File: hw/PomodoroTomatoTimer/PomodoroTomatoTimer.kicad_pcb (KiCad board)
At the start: 2 copper layers, 25.4 x 25.4 mm, 19 parts, among them J1 Coin Cell, SW1 SW_DIP_x02, U1 STM32F030F4Px

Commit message: + Placement and routing ok.
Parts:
- added Q1: BSS83P, Package_TO_SOT_SMD:SOT-23, F.Cu at (130.8, 88.6)
- added Q2: 2N7002, Package_TO_SOT_SMD:SOT-23, F.Cu at (129.3, 85.1)
- added Q3: BC807, Package_TO_SOT_SMD:SOT-23, F.Cu at (135.9, 97.8)
- added Q4: BSS83P, Package_TO_SOT_SMD:SOT-23, F.Cu at (139.4, 97.8)
- added Q5: BC807, Package_TO_SOT_SMD:SOT-23, F.Cu at (143.0, 97.8)
- added R10: 47k 0603, Resistor_SMD:R_0603_1608Metric, F.Cu at (133.3, 99.5)
- added R11: 10k 0603, Resistor_SMD:R_0603_1608Metric, F.Cu at (131.7, 85.2)
- added R12: 47k 0603, Resistor_SMD:R_0603_1608Metric, F.Cu at (139.2, 100.3)
- added R8: 10k 0603, Resistor_SMD:R_0603_1608Metric, F.Cu at (128.3, 88.9)
- added R9: 10k 0603, Resistor_SMD:R_0603_1608Metric, F.Cu at (135.9, 100.3)
- SW1: value SW_DIP_x02 -> SW_DPST_x2
- moved C4 23.2 mm to (128.8, 94.1), turned to 45 degrees
- moved C3 18.9 mm to (129.3, 95.6), turned to 45 degrees
- moved R1 18.1 mm to (147.7, 98.7)
- moved R2 17.1 mm to (145.4, 99.2), turned to 90 degrees
- moved D4 15.6 mm to (144.3, 79.2), turned to 270 degrees
- moved D5 15.1 mm to (148.8, 79.2), turned to 270 degrees
- moved R7 14.0 mm to (150.9, 79.2), turned to 270 degrees
- moved C1 12.9 mm to (142.5, 94.5), turned to 270 degrees
- moved U1 12.3 mm to (148.3, 93.8)
- moved C2 11.4 mm to (143.9, 94.5), turned to 270 degrees
- moved SW1 10.5 mm to (136.7, 86.4)
- moved J1 9.20 mm to (130.6, 98.0), turned to 45 degrees
- moved D3 6.03 mm to (139.7, 79.2), turned to 270 degrees
- moved D2 5.98 mm to (135.1, 79.2), turned to 270 degrees
- moved R3 5.70 mm to (132.6, 79.2), turned to 270 degrees
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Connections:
- SW1 pad 1: Net-(SW1-Pad1) -> VDDA
- SW1 pad 2: Net-(SW1-Pad2) -> /BUTTON
- U1 pad 11: Net-(U1-Pad11) -> /LED5
- U1 pad 12: Net-(U1-Pad12) -> /LED4
- U1 pad 13: Net-(U1-Pad13) -> /LED3
- U1 pad 14: Net-(U1-Pad14) -> /LED2
- U1 pad 17: Net-(U1-Pad17) -> /LED1
- U1 pad 20: Net-(U1-Pad20) -> /BUTTON
- U1 pad 6: Net-(U1-Pad6) -> /POW_CTRL
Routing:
- net VDD: track 0.00 -> 40.0 mm, vias 0 -> 2
- net /POW_CTRL: track 0.00 -> 29.3 mm, vias 0 -> 2
- net VDDA: track 0.00 -> 26.6 mm
- net GND: track 0.00 -> 25.3 mm, vias 0 -> 10
- net /BUTTON: track 0.00 -> 21.4 mm
- net /LED1: track 0.00 -> 20.6 mm
- net /LED2: track 0.00 -> 20.4 mm
- net /LED3: track 0.00 -> 16.5 mm
- net /LED4: track 0.00 -> 12.6 mm
- net Net-(Q3-Pad1): track 0.00 -> 11.9 mm, vias 0 -> 2
- net /LED5: track 0.00 -> 11.0 mm
- net Net-(Q4-Pad1): track 0.00 -> 7.94 mm
- net Net-(Q1-Pad1): track 0.00 -> 4.71 mm
- net Net-(D5-Pad2): track 0.00 -> 2.75 mm
- net Net-(D4-Pad2): track 0.00 -> 2.75 mm
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- added copper zone on B.Cu, net GND
- added copper zone on F.Cu, net GND
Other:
- net class Default: clearance 0.2 -> 0.25
- rule trace_clearance: 0.2 -> 0.25

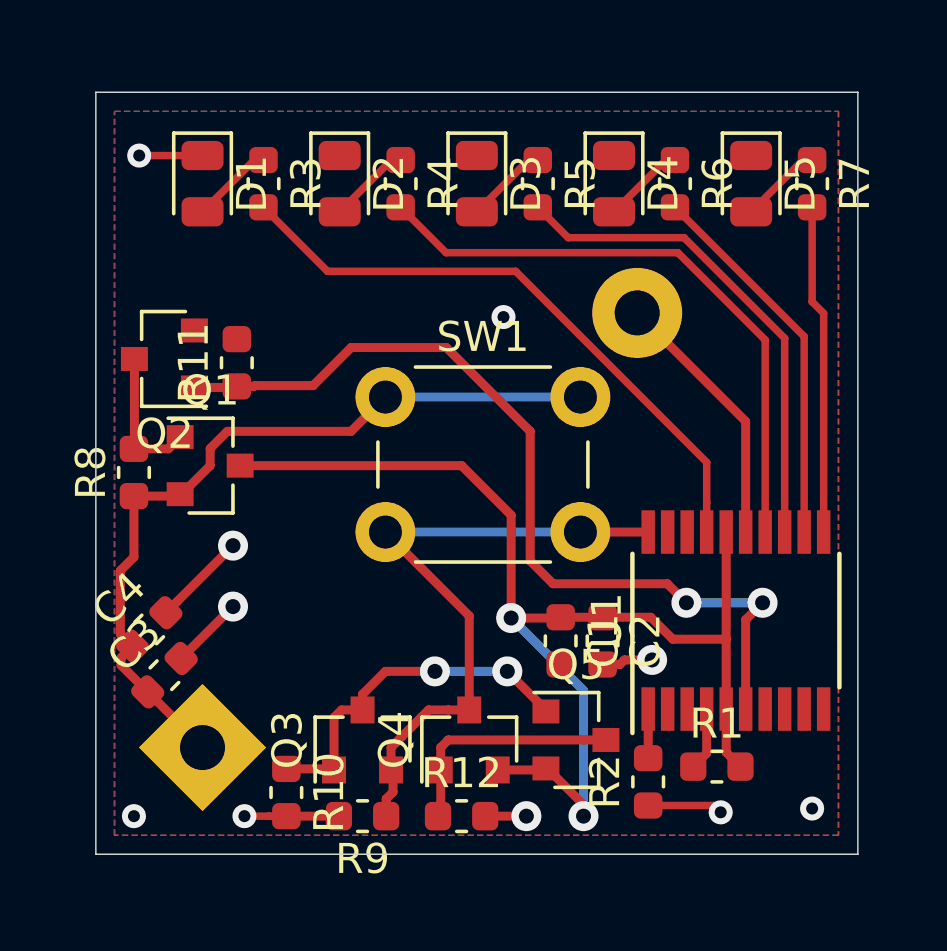
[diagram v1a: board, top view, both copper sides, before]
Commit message: + silk screen updated
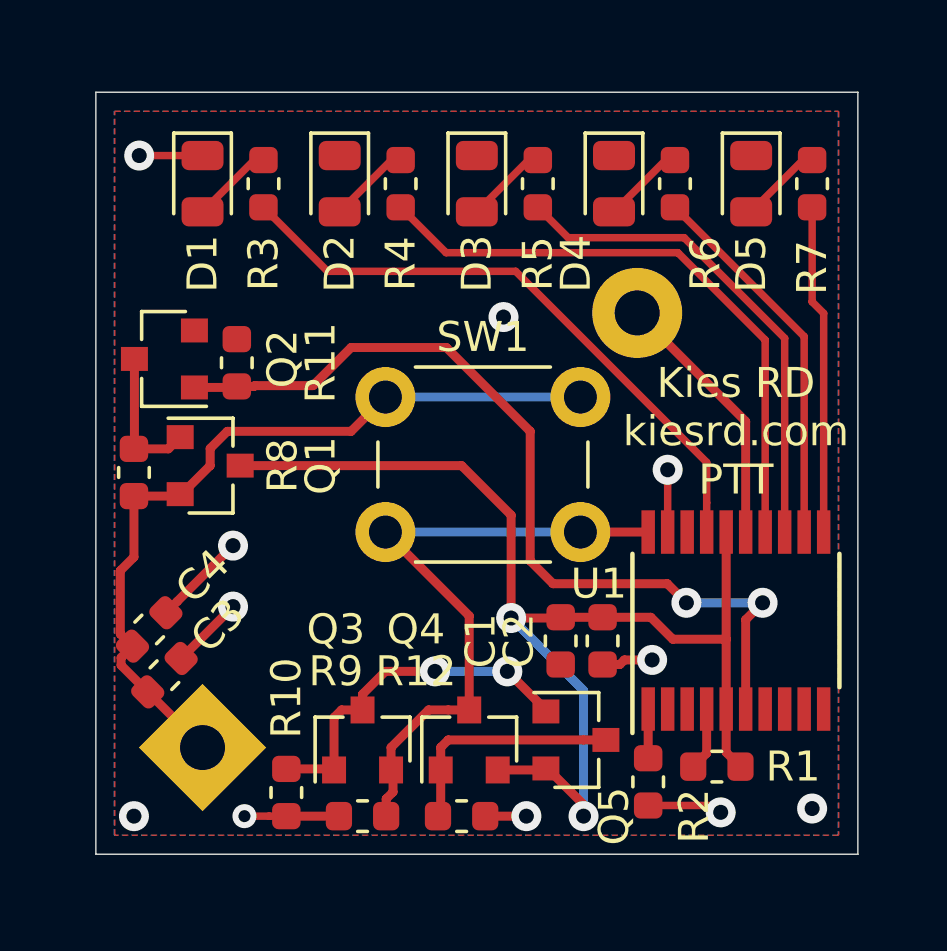
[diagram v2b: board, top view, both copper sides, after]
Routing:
- net Net-(U1-Pad19): track 0.00 -> 2.08 mm, vias 0 -> 1
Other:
- board text added: "Kies RD kiesrd.com PTT"
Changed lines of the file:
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@@
   (general
     (thickness 1.6)
-    (drawings 5)
-    (tracks 148)
+    (drawings 7)
+    (tracks 150)
     (zones 0)
     (modules 29)
@@
     (tags diode)
     (attr smd)
-    (fp_text reference D4 (at 0 -1.65 90) (layer F.SilkS)
+    (fp_text reference D4 (at 2.667 1.27 90) (layer F.SilkS)
       (effects (font (size 1 1) (thickness 0.15)))
     )
@@
     (tags resistor)
     (attr smd)
-    (fp_text reference R1 (at 0 -1.43) (layer F.SilkS)
+    (fp_text reference R1 (at 2.54 0) (layer F.SilkS)
       (effects (font (size 1 1) (thickness 0.15)))
     )
@@
     (tags resistor)
     (attr smd)
-    (fp_text reference R2 (at 0 -1.43 90) (layer F.SilkS)
+    (fp_text reference R2 (at -1.143 1.528 90) (layer F.SilkS)
       (effects (font (size 1 1) (thickness 0.15)))
     )
@@
     (tags "SSOP 0.65")
     (attr smd)
-    (fp_text reference U1 (at 0 -4.3 90) (layer F.SilkS)
+    (fp_text reference U1 (at 1.227 -4.572 180) (layer F.SilkS)
       (effects (font (size 1 1) (thickness 0.15)))
     )
@@
     (tags diode)
     (attr smd)
-    (fp_text reference D1 (at 0 -1.65 90) (layer F.SilkS)
+    (fp_text reference D1 (at 2.667 0 90) (layer F.SilkS)
       (effects (font (size 1 1) (thickness 0.15)))
     )
@@
     (tags diode)
     (attr smd)
-    (fp_text reference D2 (at 0 -1.65 90) (layer F.SilkS)
+    (fp_text reference D2 (at 2.667 0 90) (layer F.SilkS)
       (effects (font (size 1 1) (thickness 0.15)))
     )
@@
     (tags diode)
     (attr smd)
-    (fp_text reference D3 (at 0 -1.65 90) (layer F.SilkS)
+    (fp_text reference D3 (at 2.667 0 90) (layer F.SilkS)
       (effects (font (size 1 1) (thickness 0.15)))
     )
@@
     (tags diode)
     (attr smd)
-    (fp_text reference D5 (at 0 -1.65 90) (layer F.SilkS)
+    (fp_text reference D5 (at 2.667 0 90) (layer F.SilkS)
       (effects (font (size 1 1) (thickness 0.15)))
     )
@@
     (tags resistor)
     (attr smd)
-    (fp_text reference R3 (at 0 -1.43 90) (layer F.SilkS)
+    (fp_text reference R3 (at 2.667 0 90) (layer F.SilkS)
       (effects (font (size 1 1) (thickness 0.15)))
     )
@@
     (tags resistor)
     (attr smd)
-    (fp_text reference R4 (at 0 -1.43 90) (layer F.SilkS)
+    (fp_text reference R4 (at 2.667 0 90) (layer F.SilkS)
       (effects (font (size 1 1) (thickness 0.15)))
     )
@@
     (tags resistor)
     (attr smd)
-    (fp_text reference R5 (at 0 -1.43 90) (layer F.SilkS)
+    (fp_text reference R5 (at 2.667 0 90) (layer F.SilkS)
       (effects (font (size 1 1) (thickness 0.15)))
     )
@@
     (tags resistor)
     (attr smd)
-    (fp_text reference R6 (at 0 -1.43 90) (layer F.SilkS)
+    (fp_text reference R6 (at 2.667 -1.016 90) (layer F.SilkS)
       (effects (font (size 1 1) (thickness 0.15)))
     )
@@
     (tags resistor)
     (attr smd)
-    (fp_text reference R7 (at 0 -1.43 90) (layer F.SilkS)
+    (fp_text reference R7 (at 2.794 0 90) (layer F.SilkS)
       (effects (font (size 1 1) (thickness 0.15)))
     )
@@
     (tags capacitor)
     (attr smd)
-    (fp_text reference C1 (at 0 -1.43 90) (layer F.SilkS)
+    (fp_text reference C1 (at 0 2.667 90) (layer F.SilkS)
       (effects (font (size 1 1) (thickness 0.15)))
     )
@@
     (tags capacitor)
     (attr smd)
-    (fp_text reference C2 (at 0 -1.43 90) (layer F.SilkS)
+    (fp_text reference C2 (at 0 2.794 90) (layer F.SilkS)
       (effects (font (size 1 1) (thickness 0.15)))
     )
@@
     (tags capacitor)
     (attr smd)
-    (fp_text reference C3 (at 0 -1.43 45) (layer F.SilkS)
+    (fp_text reference C3 (at 2.424669 0.089803 45) (layer F.SilkS)
       (effects (font (size 1 1) (thickness 0.15)))
     )
@@
     (tags capacitor)
     (attr smd)
-    (fp_text reference C4 (at 0 -1.43 45) (layer F.SilkS)
+    (fp_text reference C4 (at 2.514472 0 45) (layer F.SilkS)
       (effects (font (size 1 1) (thickness 0.15)))
     )
@@
     (descr http://www.keyelco.com/product-pdf.cfm?p=719)
     (tags "Keystone type 103 battery holder")
-    (fp_text reference J1 (at 0 4.3 45) (layer B.SilkS)
+    (fp_text reference J1 (at 3.053287 4.130918 45) (layer B.SilkS)
       (effects (font (size 1 1) (thickness 0.15)) (justify mirror))
     )
@@
     (tags SOT-23)
     (attr smd)
-    (fp_text reference Q1 (at 0 -2.5) (layer F.SilkS)
+    (fp_text reference Q1 (at 3.683 0 90) (layer F.SilkS)
       (effects (font (size 1 1) (thickness 0.15)))
     )
@@
     (tags SOT-23)
     (attr smd)
-    (fp_text reference Q2 (at 0 -2.5) (layer F.SilkS)
+    (fp_text reference Q2 (at -3.937 0 90) (layer F.SilkS)
       (effects (font (size 1 1) (thickness 0.15)))
     )
@@
     (tags resistor)
     (attr smd)
-    (fp_text reference R8 (at 0 -1.43 90) (layer F.SilkS)
+    (fp_text reference R8 (at 0.2285 4.953 90) (layer F.SilkS)
       (effects (font (size 1 1) (thickness 0.15)))
     )
@@
     (tags resistor)
     (attr smd)
-    (fp_text reference R11 (at 0 -1.43 90) (layer F.SilkS)
+    (fp_text reference R11 (at 0 2.794 90) (layer F.SilkS)
       (effects (font (size 1 1) (thickness 0.15)))
     )
@@
     (tags SOT-23)
     (attr smd)
-    (fp_text reference Q3 (at 0 -2.5 90) (layer F.SilkS)
+    (fp_text reference Q3 (at 3.683 -0.889 180) (layer F.SilkS)
       (effects (font (size 1 1) (thickness 0.15)))
     )
@@
     (tags SOT-23)
     (attr smd)
-    (fp_text reference Q4 (at 0 -2.5 90) (layer F.SilkS)
+    (fp_text reference Q4 (at 3.683 -1.778 180) (layer F.SilkS)
       (effects (font (size 1 1) (thickness 0.15)))
     )
@@
     (tags SOT-23)
     (attr smd)
-    (fp_text reference Q5 (at 0 -2.5) (layer F.SilkS)
+    (fp_text reference Q5 (at 1.27 2.54 90) (layer F.SilkS)
       (effects (font (size 1 1) (thickness 0.15)))
     )
@@
     (tags resistor)
     (attr smd)
-    (fp_text reference R9 (at 0 -1.43 180) (layer F.SilkS)
+    (fp_text reference R9 (at 0.889 4.826 180) (layer F.SilkS)
       (effects (font (size 1 1) (thickness 0.15)))
     )
@@
     (tags resistor)
     (attr smd)
-    (fp_text reference R10 (at 0 -1.43 90) (layer F.SilkS)
+    (fp_text reference R10 (at -3.1495 0 90) (layer F.SilkS)
       (effects (font (size 1 1) (thickness 0.15)))
     )
@@
     (tags resistor)
     (attr smd)
-    (fp_text reference R12 (at 0 -1.43) (layer F.SilkS)
+    (fp_text reference R12 (at -1.524 -4.826) (layer F.SilkS)
       (effects (font (size 1 1) (thickness 0.15)))
     )
@@
       (rotate (xyz 0 0 0))
     )
+  )
+  (gr_circle (center 146.05 88.773) (end 146.35 88.773) (layer F.Mask) (width 0.5))
+  (gr_text "Kies RD\nkiesrd.com\nPTT" (at 148.336 87.503) (layer F.SilkS)
+    (effects (font (size 1 1) (thickness 0.15)))
   )
   (dimension 25.4 (width 0.15) (layer Eco1.User)
@@
   (gr_line (start 127 76.2) (end 152.4 76.2) (layer Edge.Cuts) (width 0.05))
   (gr_line (start 127 101.6) (end 127 76.2) (layer Edge.Cuts) (width 0.05))
-  (via (at 128.27 100.33) (size 0.8) (drill 0.4) (layers F.Cu B.Cu) (net 3))
-  (via (at 150.876 100.076) (size 0.8) (drill 0.4) (layers F.Cu B.Cu) (net 3))
-  (via (at 140.589 83.693) (size 0.8) (drill 0.4) (layers F.Cu B.Cu) (net 3))
+  (via (at 128.27 100.33) (size 1) (drill 0.5) (layers F.Cu B.Cu) (net 3))
+  (via (at 150.876 100.076) (size 1) (drill 0.5) (layers F.Cu B.Cu) (net 3))
+  (via (at 140.589 83.693) (size 1) (drill 0.5) (layers F.Cu B.Cu) (net 3))
   (segment (start 148.011 98.2015) (end 148.011 96.76) (width 0.3) (layer F.Cu) (net 1))
   (segment (start 148.4885 98.679) (end 148.011 98.2015) (width 0.3) (layer F.Cu) (net 1))
@@
   (segment (start 129.714916 93.170084) (end 131.572 91.313) (width 0.3) (layer F.Cu) (net 3))
   (segment (start 130.556 78.3105) (end 128.4455 78.3105) (width 0.25) (layer F.Cu) (net 3))
-  (via (at 128.4455 78.3105) (size 0.8) (drill 0.4) (layers F.Cu B.Cu) (net 3))
+  (via (at 128.4455 78.3105) (size 1) (drill 0.5) (layers F.Cu B.Cu) (net 3))
   (segment (start 133.35 100.33) (end 132.775 100.33) (width 0.25) (layer F.Cu) (net 3))
   (via (at 131.953 100.33) (size 0.8) (drill 0.4) (layers F.Cu B.Cu) (net 3))
   (segment (start 132.775 100.33) (end 131.953 100.33) (width 0.25) (layer F.Cu) (net 3))
   (segment (start 145.411 99.9745) (end 147.5995 99.9745) (width 0.25) (layer F.Cu) (net 3))
-  (via (at 147.828 100.203) (size 0.8) (drill 0.4) (layers F.Cu B.Cu) (net 3))
+  (via (at 147.828 100.203) (size 1) (drill 0.5) (layers F.Cu B.Cu) (net 3))
   (segment (start 147.5995 99.9745) (end 147.828 100.203) (width 0.25) (layer F.Cu) (net 3))
   (segment (start 145.411 98.3995) (end 145.411 96.76) (width 0.3) (layer F.Cu) (net 4))
+  (segment (start 146.061 90.86) (end 146.061 88.784) (width 0.25) (layer F.Cu) (net 12))
+  (via (at 146.061 88.784) (size 1) (drill 0.5) (layers F.Cu B.Cu) (net 12))
   (segment (start 132.281 78.4605) (end 132.588 78.4605) (width 0.25) (layer F.Cu) (net 13))
   (segment (start 130.556 80.1855) (end 132.281 78.4605) (width 0.25) (layer F.Cu) (net 13))

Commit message: + 3D Box
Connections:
- U1 pad 18: Net-(U1-Pad18) -> /BUTTON
- U1 pad 20: /BUTTON -> Net-(U1-Pad20)
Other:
- board text added: "Kies RD kiesrd.com -PTT-"
- board text removed: "Kies RD kiesrd.com PTT"

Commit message: + 3D Updated. Empty software project created
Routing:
- net /BUTTON: track 21.4 -> 24.3 mm
- net Net-(U1-Pad20): track 0.00 -> 2.51 mm, vias 0 -> 1
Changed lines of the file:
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@@
   (general
     (thickness 1.6)
-    (drawings 7)
-    (tracks 150)
+    (drawings 8)
+    (tracks 157)
     (zones 0)
     (modules 29)
@@
     )
   )
+  (gr_circle (center 144.399 88.773) (end 144.699 88.773) (layer F.Mask) (width 0.5))
   (gr_circle (center 146.05 88.773) (end 146.35 88.773) (layer F.Mask) (width 0.5))
   (gr_text "Kies RD\nkiesrd.com\n-PTT-" (at 148.336 87.503) (layer F.SilkS)
@@
   (segment (start 148.661 93.782) (end 149.225 93.218) (width 0.3) (layer F.Cu) (net 24))
   (segment (start 148.661 96.76) (end 148.661 93.782) (width 0.3) (layer F.Cu) (net 24))
-  (segment (start 141.478 91.821) (end 142.24 92.583) (width 0.3) (layer F.Cu) (net 24))
+  (segment (start 146.177 92.71) (end 146.685 93.218) (width 0.3) (layer F.Cu) (net 24))
+  (segment (start 142.367 92.71) (end 146.177 92.71) (width 0.3) (layer F.Cu) (net 24))
+  (segment (start 141.478 91.821) (end 142.367 92.71) (width 0.3) (layer F.Cu) (net 24))
   (segment (start 141.478 87.503) (end 141.478 91.821) (width 0.3) (layer F.Cu) (net 24))
   (segment (start 132.274 86.0045) (end 132.2995 85.979) (width 0.3) (layer F.Cu) (net 24))
   (segment (start 131.699 86.0045) (end 132.274 86.0045) (width 0.3) (layer F.Cu) (net 24))
-  (segment (start 146.05 92.583) (end 146.685 93.218) (width 0.3) (layer F.Cu) (net 24))
   (segment (start 132.2995 85.979) (end 134.239 85.979) (width 0.3) (layer F.Cu) (net 24))
   (segment (start 134.239 85.979) (end 135.509 84.709) (width 0.3) (layer F.Cu) (net 24))
   (segment (start 135.509 84.709) (end 138.684 84.709) (width 0.3) (layer F.Cu) (net 24))
-  (segment (start 142.24 92.583) (end 146.05 92.583) (width 0.3) (layer F.Cu) (net 24))
   (segment (start 138.684 84.709) (end 141.478 87.503) (width 0.3) (layer F.Cu) (net 24))
   (segment (start 134.905 98.755) (end 134.94 98.79) (width 0.3) (layer F.Cu) (net 25))
@@
   (segment (start 139.446 96.79) (end 139.446 93.654) (width 0.3) (layer F.Cu) (net 26))
   (segment (start 136.652 90.86) (end 143.152 90.86) (width 0.3) (layer B.Cu) (net 26) (status C00000))
-  (segment (start 143.152 90.86) (end 145.411 90.86) (width 0.3) (layer F.Cu) (net 26) (status C00000))
+  (segment (start 146.711 91.835) (end 146.711 90.86) (width 0.25) (layer F.Cu) (net 26))
+  (segment (start 146.471 92.075) (end 146.711 91.835) (width 0.25) (layer F.Cu) (net 26))
+  (segment (start 144.367 92.075) (end 146.471 92.075) (width 0.25) (layer F.Cu) (net 26))
+  (segment (start 143.152 90.86) (end 144.367 92.075) (width 0.25) (layer F.Cu) (net 26))
   (segment (start 138.496 100.2385) (end 138.4045 100.33) (width 0.3) (layer F.Cu) (net 27))
   (segment (start 138.496 98.79) (end 138.496 100.2385) (width 0.3) (layer F.Cu) (net 27))
@@
   (segment (start 138.496 98.04) (end 138.746 97.79) (width 0.3) (layer F.Cu) (net 27))
   (segment (start 138.496 98.79) (end 138.496 98.04) (width 0.3) (layer F.Cu) (net 27))
+  (segment (start 145.411 90.36) (end 144.399 89.348) (width 0.25) (layer F.Cu) (net 28))
+  (segment (start 145.411 90.86) (end 145.411 90.36) (width 0.25) (layer F.Cu) (net 28))
+  (via (at 144.399 88.773) (size 1) (drill 0.5) (layers F.Cu B.Cu) (net 28))
+  (segment (start 144.399 89.348) (end 144.399 88.773) (width 0.25) (layer F.Cu) (net 28))
   (zone (net 3) (net_name GND) (layer F.Cu) (hatch edge 0.508)
     (connect_pads (clearance 0.508))
